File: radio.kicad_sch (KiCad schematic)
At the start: 35 parts, among them Q1 BSS138W-7-F, U3 SX1276, X1 AS183-92LF, Y1 ECS-TXO-25CSMV-320-AM-TR

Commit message: proper formating
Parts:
- removed U3: SX1276, Package_DFN_QFN:QFN-28-1EP_6x6mm_P0.65mm_EP4.8x4.8mm, symbol RF:SX1276
- added U2, U3: SX1276IMLTRT, SMTC-QFN-28_V, symbol Altium Content Vault:root_0_SMTC-SX127X-QFN-28_Altium Content Vault
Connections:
- net 3V3: now also U3.10 (DIO2/DATA), U3.8 (DIO0), U3.9 (DIO1/DCLK)
- net CS: now also U2.19 (NSS)
- net LORA_RXTX: now also U2.20 (RXTX/RF_MOD)
- net MISO: now also U2.17 (MISO)
- net MOSI: now also U2.18 (MOSI)
- net NRST_WL: now also U2.7 (NRESET)
- net PA_BOOST: now also U2.27 (PA_BOOST)
- net SCK: now also U2.16 (SCK)
- net VR_PA: now also U3.13 (DIO5)
- net at C7.1, L1.2: now also U2.1 (RFI_LF)
- net at C8.1, C8.2, Y1.3 (OUTPUT): now also U2.5 (XTA)
- net at C21.1: now also U3.11 (DIO3)
- net at C22.1: now also U3.12 (DIO4)
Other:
- moved on the sheet: C11, C21, C22, C8, L4, Y1

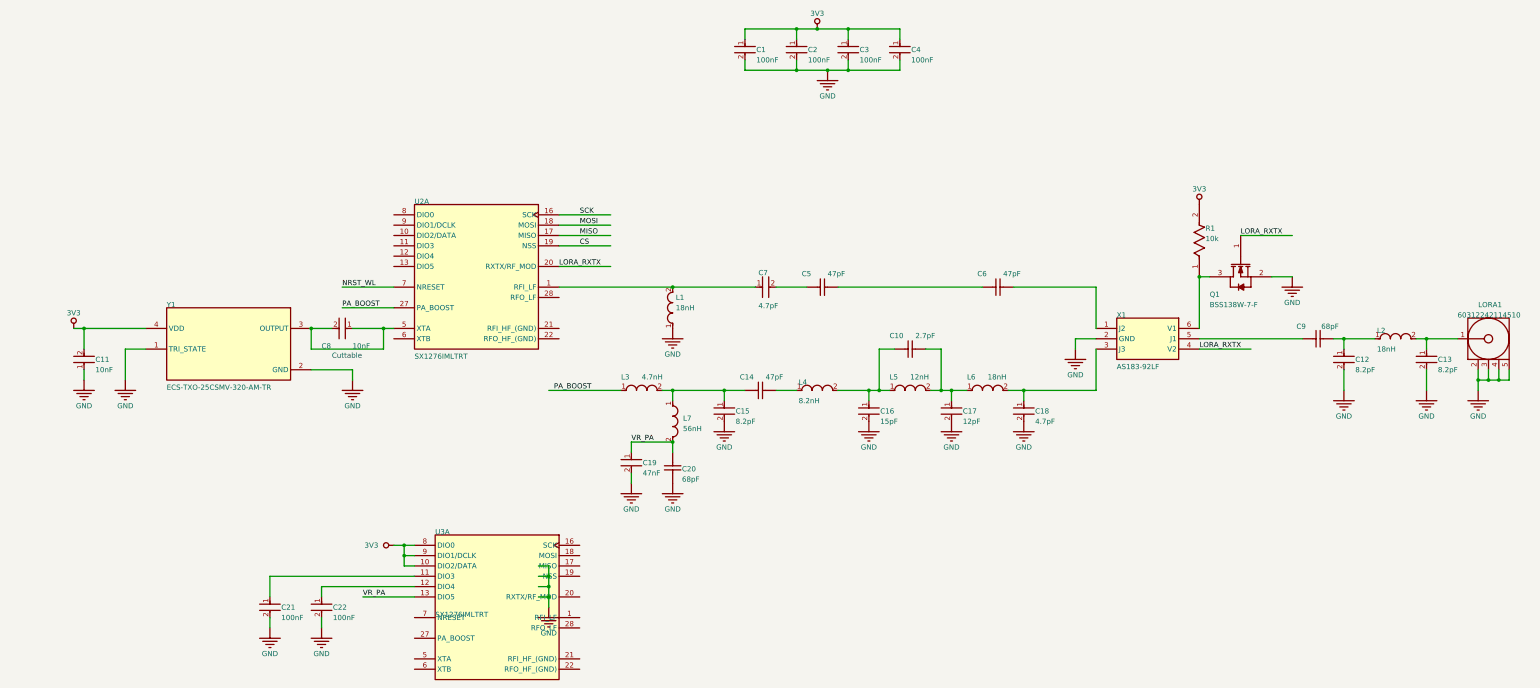
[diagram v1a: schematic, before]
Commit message: Add power supply voltage cutoff, start fixing radio schematic
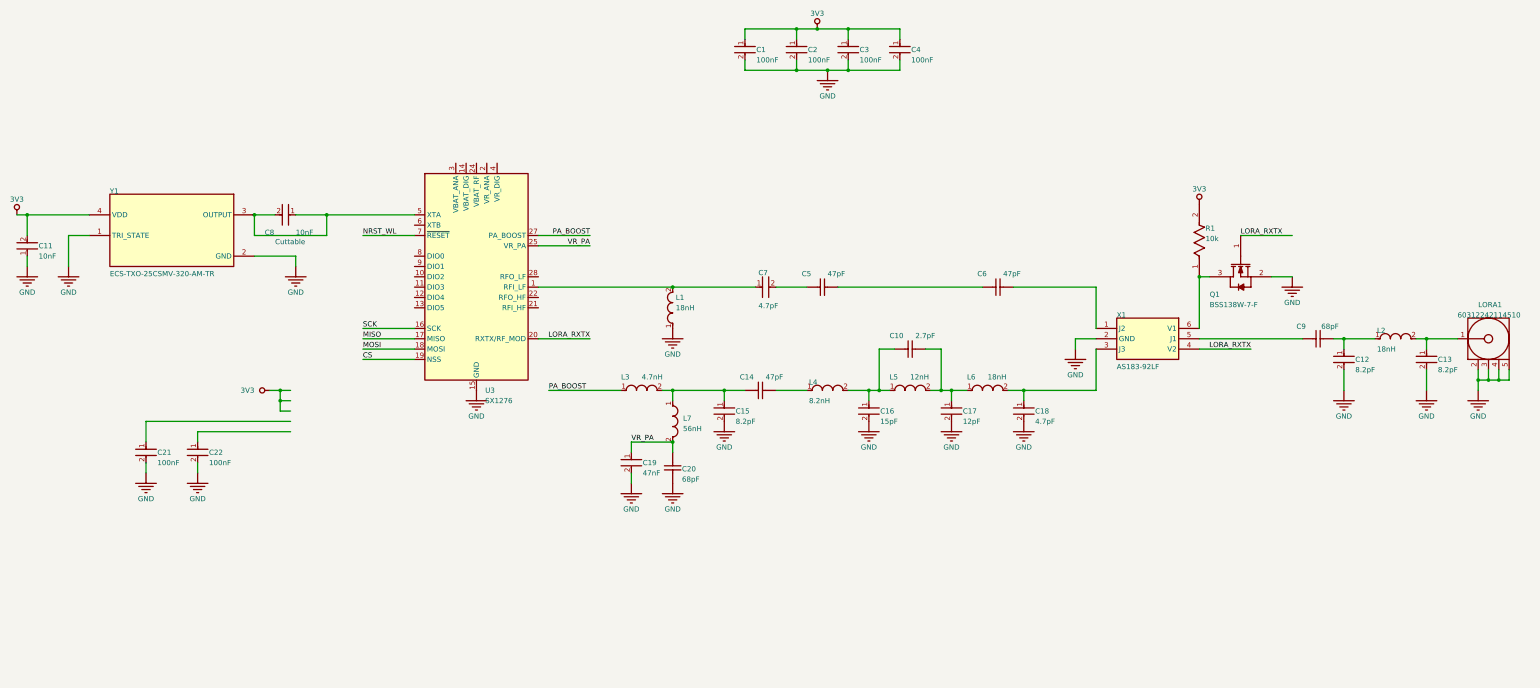
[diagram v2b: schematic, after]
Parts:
- removed U2, U3: SX1276IMLTRT, SMTC-QFN-28_V, symbol Altium Content Vault:root_0_SMTC-SX127X-QFN-28_Altium Content Vault
- added U3: SX1276, Package_DFN_QFN:QFN-28-1EP_6x6mm_P0.65mm_EP4.8x4.8mm, symbol RF:SX1276
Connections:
- net CS: now also U3.19 (NSS)
- net GND: now also U3.15 (GND), U3.23 (GND), U3.26 (GND), U3.29 (GND)
- net LORA_RXTX: now also U3.20 (RXTX/RF_MOD)
- net MISO: now also U3.17 (MISO)
- net MOSI: now also U3.18 (MOSI)
- net NRST_WL: now also U3.7 (~{RESET})
- net PA_BOOST: now also U3.27 (PA_BOOST)
- net SCK: now also U3.16 (SCK)
- net VR_PA: now also U3.25 (VR_PA)
- net at C7.1, L1.2: now also U3.1 (RFI_LF)
- net at C8.1, C8.2, Y1.3 (OUTPUT): now also U3.5 (XTA)
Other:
- moved on the sheet: C11, C21, C22, C8, L4, Y1
